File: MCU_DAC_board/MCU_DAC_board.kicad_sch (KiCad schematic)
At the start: 43 parts, among them J11 105-0752-001, J12 Conn_01x03_Pin, J5 54-00127, J6 105-0752-001, J7 Screw_Terminal_01x02, J8 Screw_Terminal_01x02, Q1 FZT953, U1 ADAU1966AWBSTZ, U2 ESP32-S3-DEVKITC-1-N8R2, U3 ESP32-S3-DEVKITC-1-N8R2

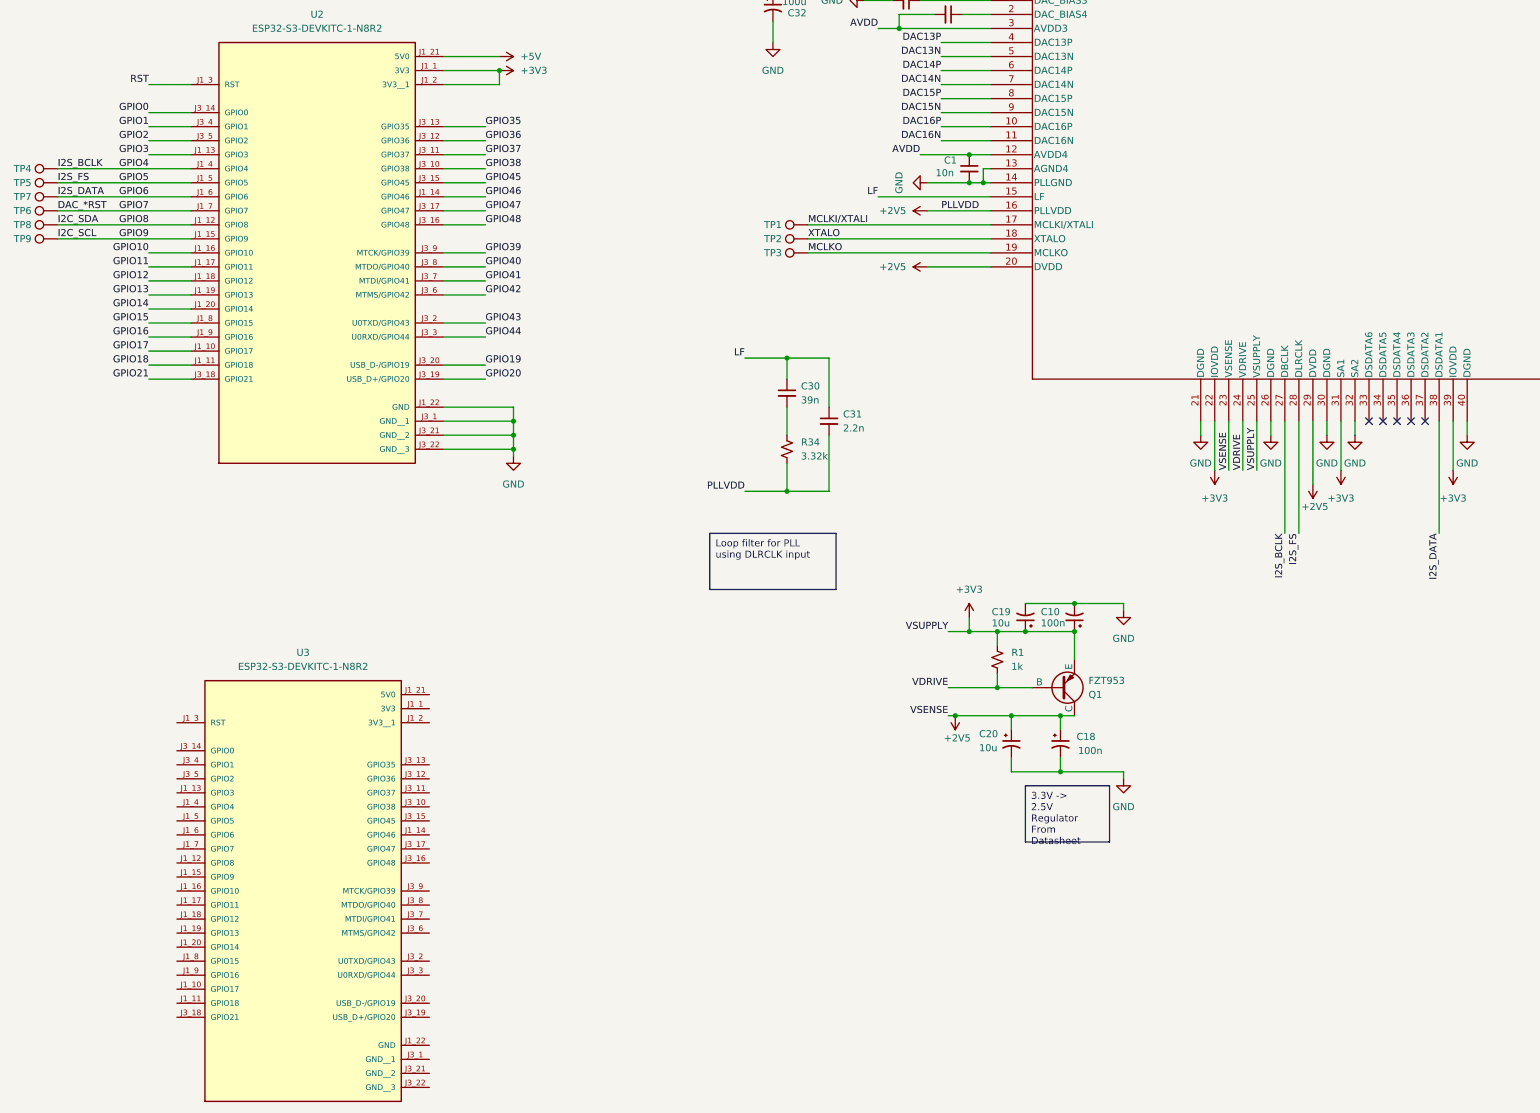
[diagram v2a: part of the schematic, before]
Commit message: Changed to 4 layer board
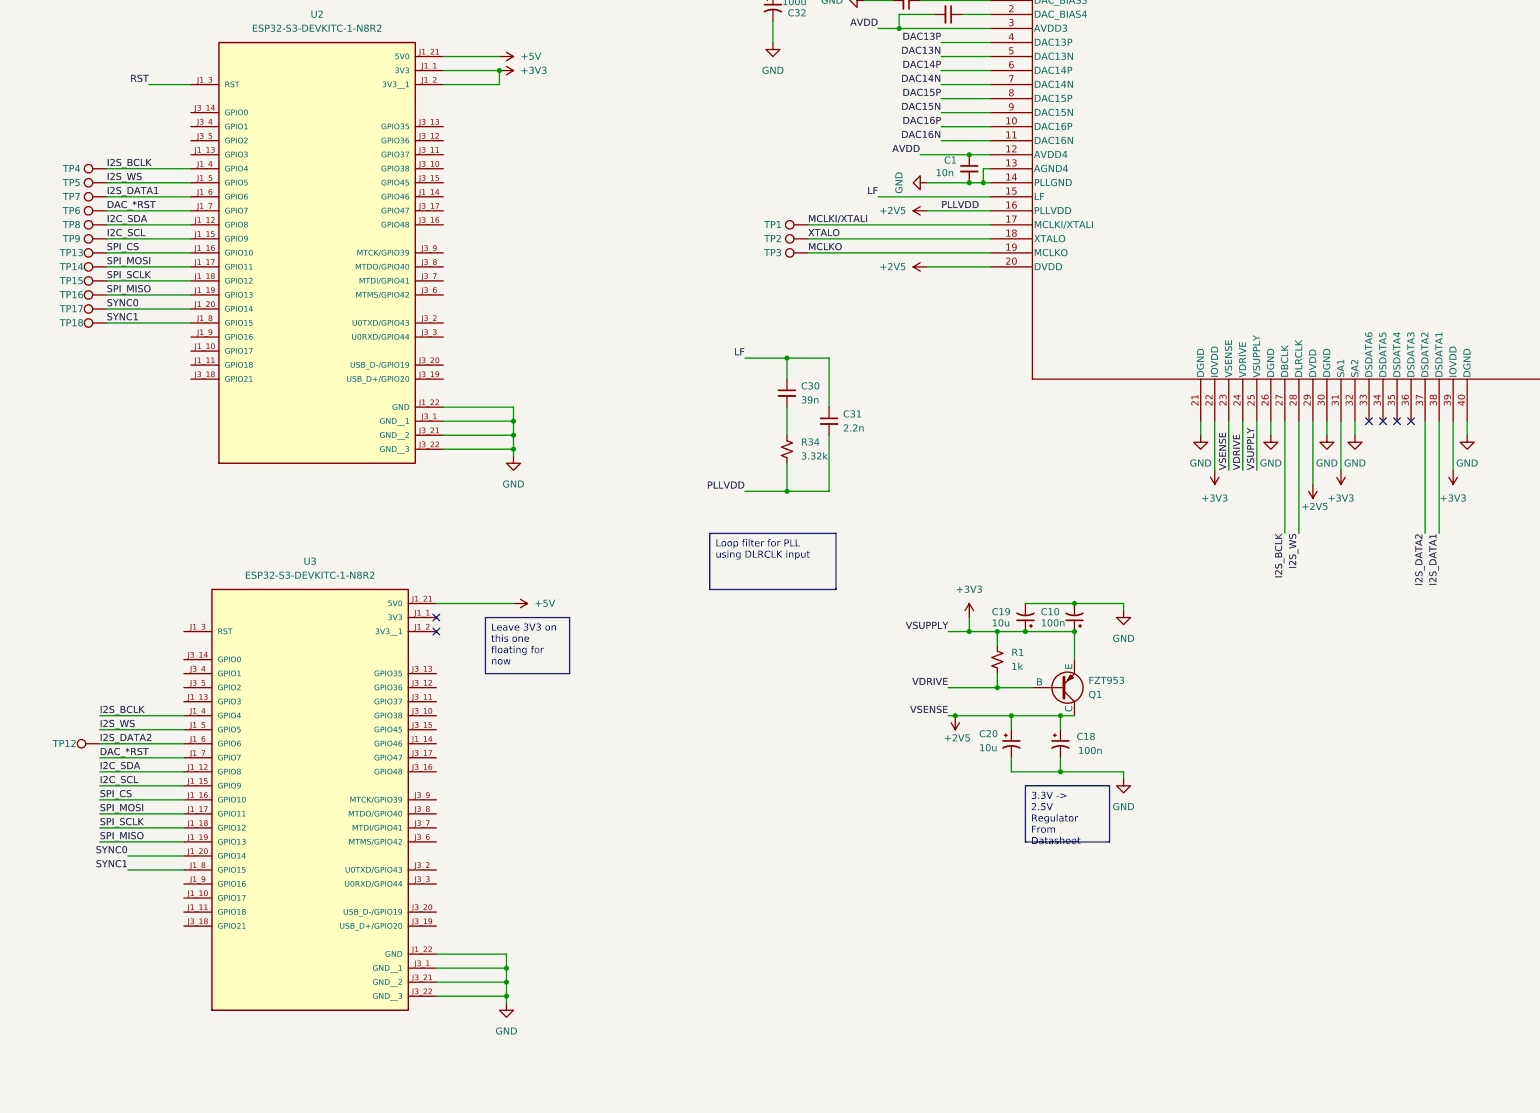
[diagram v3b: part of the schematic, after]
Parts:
- added TP12: I2S_DATA2, project_lib:TP_1.8x1mm, symbol Connector:TestPoint
- added TP13: SPI_CS, project_lib:TP_1.8x1mm, symbol Connector:TestPoint
- added TP14: SPI_MOSI, project_lib:TP_1.8x1mm, symbol Connector:TestPoint
- added TP15: SPI_SCLK, project_lib:TP_1.8x1mm, symbol Connector:TestPoint
- added TP16: SPI_MISO, project_lib:TP_1.8x1mm, symbol Connector:TestPoint
- added TP17: SYNC0, project_lib:TP_1.8x1mm, symbol Connector:TestPoint
- added TP18: SYNC1, project_lib:TP_1.8x1mm, symbol Connector:TestPoint
- TP5: value I2S_FS -> I2S_WS
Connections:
- net GPIO10 is gone; now on net SPI_CS: U2.J1_16 (GPIO10)
- net GPIO11 is gone; now on net SPI_MOSI: U2.J1_17 (GPIO11)
- net GPIO12 is gone; now on net SPI_SCLK: U2.J1_18 (GPIO12)
- net GPIO13 is gone; now on net SPI_MISO: U2.J1_19 (GPIO13)
- net GPIO14 is gone; now on net SYNC0: U2.J1_20 (GPIO14)
- net GPIO15 is gone; now on net SYNC1: U2.J1_8 (GPIO15)
- net GPIO4 is gone; now on net I2S_BCLK: TP4.1, U1.27 (DBCLK), U2.J1_4 (GPIO4)
- net GPIO5 is gone; now on net I2S_WS: TP5.1, U1.28 (DLRCLK), U2.J1_5 (GPIO5)
- net GPIO8 is gone; now on net I2C_SDA: R35.2, TP8.1, U1.43 (MISO/SDA/SA), U2.J1_12 (GPIO8)
- net GPIO9 is gone; now on net I2C_SCL: R37.2, TP9.1, U1.44 (SCLK/SCL), U2.J1_15 (GPIO9)
- net +2V5: now also Q1.2 (C); no longer Q1.1 (C)
- net +5V: now also U3.J1_21 (5V0)
- net DAC_*RST: now also U3.J1_7 (GPIO7)
- net GND: now also U3.J1_22 (GND), U3.J3_1 (GND__1), U3.J3_21 (GND__2), U3.J3_22 (GND__3)
- net VDRIVE: now also Q1.1 (B); no longer Q1.2 (B)
- net I2C_SDA: now reaches U3.J1_12 (GPIO8)
- net I2C_SCL: now reaches U3.J1_15 (GPIO9)
- net SPI_CS: now reaches U3.J1_16 (GPIO10)
- net SPI_CS: now also TP13.1
- net SPI_MOSI: now reaches U3.J1_17 (GPIO11)
- net SPI_MOSI: now also TP14.1
- net SPI_SCLK: now reaches U3.J1_18 (GPIO12)
- net SPI_SCLK: now also TP15.1
- net SPI_MISO: now reaches U3.J1_19 (GPIO13)
- net SPI_MISO: now also TP16.1
- net SYNC0: now reaches U3.J1_20 (GPIO14)
- net SYNC0: now also TP17.1
- net I2S_BCLK: now reaches U3.J1_4 (GPIO4)
- net I2S_WS: now reaches U3.J1_5 (GPIO5)
- net I2S_DATA2: now reaches U3.J1_6 (GPIO6)
- net I2S_DATA2: now also U1.37 (DSDATA2), TP12.1
- net SYNC1: now reaches U3.J1_8 (GPIO15)
- net SYNC1: now also TP18.1
- net GPIO0: no longer names the net of U2.J3_14 (GPIO0)
- net GPIO1: no longer names the net of U2.J3_4 (GPIO1)
- net GPIO16: no longer names the net of U2.J1_9 (GPIO16)
- net GPIO17: no longer names the net of U2.J1_10 (GPIO17)
- net GPIO18: no longer names the net of U2.J1_11 (GPIO18)
- net GPIO19: no longer names the net of U2.J3_20 (USB_D-/GPIO19)
- net GPIO2: no longer names the net of U2.J3_5 (GPIO2)
- net GPIO20: no longer names the net of U2.J3_19 (USB_D+/GPIO20)
- net GPIO21: no longer names the net of U2.J3_18 (GPIO21)
- net GPIO3: no longer names the net of U2.J1_13 (GPIO3)
- net GPIO35: no longer names the net of U2.J3_13 (GPIO35)
- net GPIO36: no longer names the net of U2.J3_12 (GPIO36)
- net GPIO37: no longer names the net of U2.J3_11 (GPIO37)
- net GPIO38: no longer names the net of U2.J3_10 (GPIO38)
- net GPIO39: no longer names the net of U2.J3_9 (MTCK/GPIO39)
- net GPIO40: no longer names the net of U2.J3_8 (MTDO/GPIO40)
- net GPIO41: no longer names the net of U2.J3_7 (MTDI/GPIO41)
- net GPIO42: no longer names the net of U2.J3_6 (MTMS/GPIO42)
- net GPIO43: no longer names the net of U2.J3_2 (U0TXD/GPIO43)
- net GPIO44: no longer names the net of U2.J3_3 (U0RXD/GPIO44)
- net GPIO45: no longer names the net of U2.J3_15 (GPIO45)
- net GPIO46: no longer names the net of U2.J1_14 (GPIO46)
- net GPIO47: no longer names the net of U2.J3_17 (GPIO47)
- net GPIO48: no longer names the net of U2.J3_16 (GPIO48)
- net GPIO6 renamed I2S_DATA1
- no-connect marks 5 -> 6
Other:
- moved on the sheet: TP4, TP5, TP6, TP7, TP8, TP9, U3

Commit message: Amp board final draft
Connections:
- net DAC_*RST: now also U2.J3_7 (MTDI/GPIO41), U3.J1_6 (GPIO6); no longer U2.J1_7 (GPIO7), U3.J1_7 (GPIO7)
- net I2C_SCL: now also U2.J3_9 (MTCK/GPIO39), U3.J1_4 (GPIO4); no longer U2.J1_15 (GPIO9), U3.J1_15 (GPIO9)
- net I2C_SDA: now also U2.J3_8 (MTDO/GPIO40), U3.J1_5 (GPIO5); no longer U2.J1_12 (GPIO8), U3.J1_12 (GPIO8)
- net I2S_BCLK: now also U2.J3_4 (GPIO1); no longer U2.J1_4 (GPIO4), U3.J1_4 (GPIO4)
- net I2S_DATA1: now also U2.J3_6 (MTMS/GPIO42); no longer U2.J1_6 (GPIO6)
- net I2S_DATA2: now also U3.J1_7 (GPIO7); no longer U3.J1_6 (GPIO6)
- net I2S_WS: now also U2.J3_5 (GPIO2); no longer U2.J1_5 (GPIO5), U3.J1_5 (GPIO5)
- net SPI_CS: no longer U2.J1_16 (GPIO10), U3.J1_16 (GPIO10)
- net SPI_MISO: no longer U2.J1_19 (GPIO13), U3.J1_19 (GPIO13)
- net SPI_MOSI: no longer U2.J1_17 (GPIO11), U3.J1_17 (GPIO11)
- net SPI_SCLK: no longer U2.J1_18 (GPIO12), U3.J1_18 (GPIO12)
- net SYNC0: no longer U2.J1_20 (GPIO14), U3.J1_20 (GPIO14)
- net SYNC1: no longer U2.J1_8 (GPIO15), U3.J1_8 (GPIO15)
- net USART_RX: now reaches U3.J3_2 (U0TXD/GPIO43)
- net USART_RX: now also U2.J3_3 (U0RXD/GPIO44)
- net USART_TX: now reaches U3.J3_3 (U0RXD/GPIO44)
- net USART_TX: now also U2.J3_2 (U0TXD/GPIO43)
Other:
- moved on the sheet: TP12, TP13, TP14, TP15, TP16, TP17, TP18, TP4, TP5, TP6, TP7, TP8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

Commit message: Revised DAC board schematic
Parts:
- removed TP12: I2S_DATA2, project_lib:TP_1.8x1mm, symbol Connector:TestPoint
- removed TP13: SPI_CS, project_lib:TP_1.8x1mm, symbol Connector:TestPoint
- removed TP14: SPI_MOSI, project_lib:TP_1.8x1mm, symbol Connector:TestPoint
- removed TP15: SPI_SCLK, project_lib:TP_1.8x1mm, symbol Connector:TestPoint
- removed TP16: SPI_MISO, project_lib:TP_1.8x1mm, symbol Connector:TestPoint
- removed TP17: SYNC0, project_lib:TP_1.8x1mm, symbol Connector:TestPoint
- removed TP18: SYNC1, project_lib:TP_1.8x1mm, symbol Connector:TestPoint
- removed TP4: I2S_BCLK, project_lib:TP_1.8x1mm, symbol Connector:TestPoint
- removed TP5: I2S_WS, project_lib:TP_1.8x1mm, symbol Connector:TestPoint
- removed TP6: DAC_*RST, project_lib:TP_1.8x1mm, symbol Connector:TestPoint
- removed TP7: I2S_DATA, project_lib:TP_1.8x1mm, symbol Connector:TestPoint
- removed TP8: I2C_SDA, project_lib:TP_1.8x1mm, symbol Connector:TestPoint
- removed TP9: I2C_SCL, project_lib:TP_1.8x1mm, symbol Connector:TestPoint
- removed U2, U3: ESP32-S3-DEVKITC-1-N8R2, project_lib:XCVR_ESP32-S3-DEVKITC-1-N8R2, symbol project_lib:ESP32-S3-DEVKITC-1-N8R2
- added H1, H2, H3, H4: MountingHole_Pad, symbol Mechanical:MountingHole_Pad
- added J9: Conn_02x20_Odd_Even, Connector_PinSocket_2.54mm:PinSocket_2x20_P2.54mm_Vertical_SMD, symbol Connector_Generic:Conn_02x20_Odd_Even
- added JP1: SolderJumper_2_Open, symbol Jumper:SolderJumper_2_Open
- added TP19: UART0_TX, project_lib:TP_1.8x1mm, symbol Connector:TestPoint
- added TP20: UART0_RX, project_lib:TP_1.8x1mm, symbol Connector:TestPoint
- added TP21: UART1_TX, project_lib:TP_1.8x1mm, symbol Connector:TestPoint
- added TP22: UART1_RX, project_lib:TP_1.8x1mm, symbol Connector:TestPoint
- added TP23: GPIO5, project_lib:TP_1.8x1mm, symbol Connector:TestPoint
- added TP24: I2C_SCL, project_lib:TP_1.8x1mm, symbol Connector:TestPoint
- added TP25: GPIO6, project_lib:TP_1.8x1mm, symbol Connector:TestPoint
- added TP26: I2S_BCLK, project_lib:TP_1.8x1mm, symbol Connector:TestPoint
- added TP27: I2S_DATA, project_lib:TP_1.8x1mm, symbol Connector:TestPoint
- added TP28: DAC_~{RST}, project_lib:TP_1.8x1mm, symbol Connector:TestPoint
- added TP29: XTALO, project_lib:TP_1.8x1mm, symbol Connector:TestPoint
- added TP30: MCLKO, project_lib:TP_1.8x1mm, symbol Connector:TestPoint
- TP1: value MCLKI/XTALI -> I2C_SDA
- TP2: value XTALO -> I2S_MCLK
- TP3: value MCLKO -> I2S_WS
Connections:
- net +3V3: no longer R35.1, R37.1
- net +5V: now also J9.1 (Pin_1), J9.3 (Pin_3)
- net GND: now also H1.1, H2.1, H3.1, H4.1, J9.10 (Pin_10), J9.13 (Pin_13), J9.19 (Pin_19), J9.26 (Pin_26), J9.29 (Pin_29), J9.33 (Pin_33), J9.40 (Pin_40), J9.5 (Pin_5)
- net DAC_*RST renamed DAC_~{RST}
- net DAC_~{RST}: now also J9.11 (Pin_11), TP28.1
- net I2C_SCL renamed GPIO7
- net GPIO7: now also TP1.1, U1.43 (MISO/SDA/SA), J9.4 (Pin_4); no longer U1.44 (SCLK/SCL)
- net I2C_SDA renamed GPIO8
- net GPIO8: now also U1.44 (SCLK/SCL), J9.6 (Pin_6), TP24.1; no longer U1.43 (MISO/SDA/SA)
- net I2S_BCLK renamed GPIO2
- net GPIO2: now also J9.22 (Pin_22), TP26.1
- net I2S_DATA1 renamed GPIO4
- net GPIO4: now also J9.17 (Pin_17), TP27.1
- net I2S_DATA2: no longer names the net of U1.37 (DSDATA2)
- net I2S_WS renamed GPIO3
- net GPIO3: now also TP3.1, J9.20 (Pin_20)
- net MCLKI/XTALI: no longer names the net of U1.17 (MCLKI/XTALI)
- net MCLKI/XTALI: now also JP1.2 (B); no longer TP1.1
- net MCLKO: no longer names the net of U1.19 (MCLKO)
- net MCLKO: now also TP30.1; no longer TP3.1
- net XTALO: no longer names the net of U1.18 (XTALO)
- net XTALO: now also TP29.1; no longer TP2.1
- new net +3V3_MCU: J9.18 (Pin_18), J9.2 (Pin_2), R35.1, R37.1
- new net GPIO0: J9.24 (Pin_24)
- new net GPIO1: J9.21 (Pin_21), JP1.1 (A), TP2.1
- new net GPIO20: J9.14 (Pin_14), TP21.1
- new net GPIO21: J9.12 (Pin_12), TP22.1
- new net GPIO23: J9.8 (Pin_8)
- new net GPIO24: J9.28 (Pin_28)
- new net GPIO25: J9.27 (Pin_27)
- new net GPIO26: J9.32 (Pin_32)
- new net GPIO27: J9.37 (Pin_37)
- new net GPIO32: J9.25 (Pin_25)
- new net GPIO33: J9.30 (Pin_30)
- new net GPIO36: J9.23 (Pin_23)
- new net GPIO37: J9.7 (Pin_7), TP19.1
- new net GPIO38: J9.9 (Pin_9), TP20.1
- new net GPIO45: J9.39 (Pin_39)
- new net GPIO46: J9.35 (Pin_35)
- new net GPIO47: J9.38 (Pin_38)
- new net GPIO48: J9.34 (Pin_34)
- new net GPIO5: J9.15 (Pin_15), TP23.1
- new net GPIO53: J9.36 (Pin_36)
- new net GPIO54: J9.31 (Pin_31)
- new net GPIO6: J9.16 (Pin_16), TP25.1
- no-connect marks 6 -> 5
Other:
- note added: "ADAU1966"
- note added: "Analog outputs"
- note added: "Connect to Pi"
- note added: "P4 40-pin Connector"
- note added: "TPs for Digital Signals"
- moved on the sheet: C1, C10, C18, C19, C2, C20, C3, C30, C31, C32, C4, C5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
